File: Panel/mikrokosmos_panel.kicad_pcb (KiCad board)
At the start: 2 copper layers, 200 x 25 mm, 10 parts

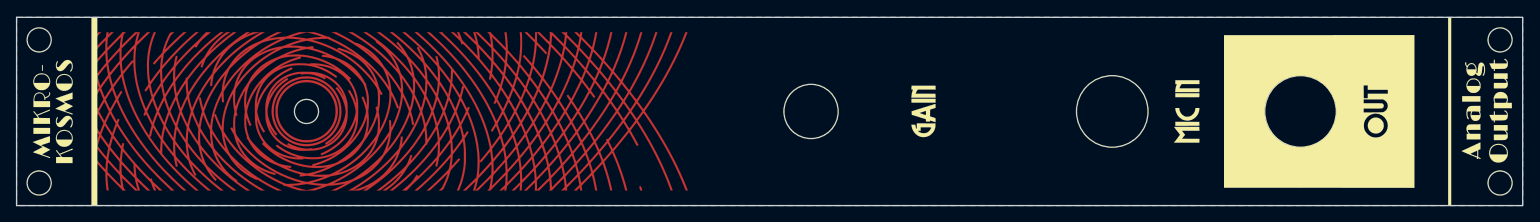
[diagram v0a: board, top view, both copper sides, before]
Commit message: Connect plane to ground via jacks
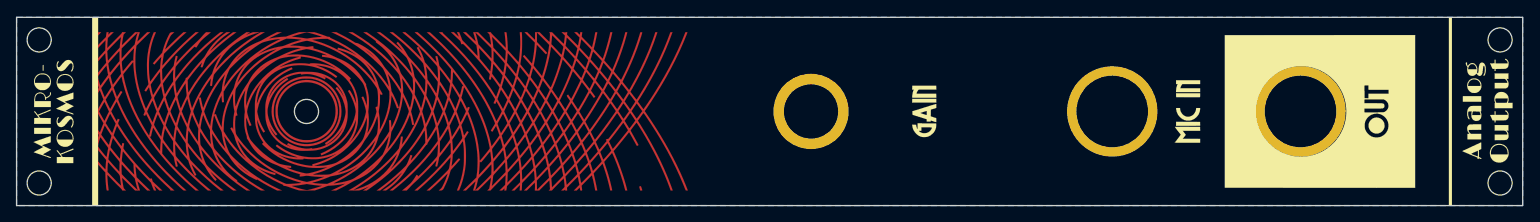
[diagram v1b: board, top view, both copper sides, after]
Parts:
- removed the G*** at (150.4, 92.5)
- removed the REF** at (220.5, 92.5)
- removed the REF** at (195.5, 92.5)
- removed the REF** at (155.5, 92.5)
- added G***: LOGO, Panel:art2, F.Cu at (150.5, 92.5)
- added H1: MountingHole_Pad, MountingHole:MountingHole_6.5mm_Pad, F.Cu at (155.5, 92.5)
- added H2: MountingHole_Pad, MountingHole:MountingHole_6.5mm_Pad, F.Cu at (195.5, 92.5)
- added H3: MountingHole_Pad, MountingHole:MountingHole_6.5mm_Pad, F.Cu at (220.5, 92.5)
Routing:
- added copper zone on B.Cu, net GND
- removed copper zone on B.Cu, net (none)
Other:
- board text removed: "JLCJLCJLCJLC"

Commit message: Front Cu fill
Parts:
- moved G*** 0.14 mm to (90.6, 92.6)
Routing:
- added copper zone on F.Cu, net GND
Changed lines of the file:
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@@
     (37 F.SilkS user)
     (38 B.Mask user)
-    (39 F.Mask user)
+    (39 F.Mask user hide)
     (40 Dwgs.User user)
     (41 Cmts.User user)
@@
   )
   (module Panel:artc (layer F.Cu)
-    (at 90.5 92.5 90)
+    (at 90.6 92.6 90)
     (fp_text reference G*** (at 0 0 90) (layer F.Cu) hide
       (effects (font (size 1.524 1.524) (thickness 0.3)))
@@
       )
     )
+  )
+  (zone (net 1) (net_name GND) (layer F.Cu) (hatch edge 0.508)
+    (connect_pads (clearance 0.508))
+    (min_thickness 0.254)
+    (fill yes (arc_segments 32) (thermal_gap 0.508) (thermal_bridge_width 0.508))
+    (polygon
+      (pts
+        (xy 250.3 105.2) (xy 49.8 105.2) (xy 49.8 79.9) (xy 250.3 79.7)
+      )
+    )
+    (polygon
+      (pts
+        (xy 60.2 103.3) (xy 139.3 103.3) (xy 139.3 81.9) (xy 60.2 81.9)
+      )
+    )
